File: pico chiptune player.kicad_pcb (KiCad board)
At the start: 4 copper layers, 80 x 70.8 mm, 31 parts, among them J1 MicroSD, J2 Speaker Out, SW1 Play / Pause, SW2 Next, SW3 Previous, U1 AY-3-8910, U2 PAM8302AAS, U3 0.96"OLED_I2C

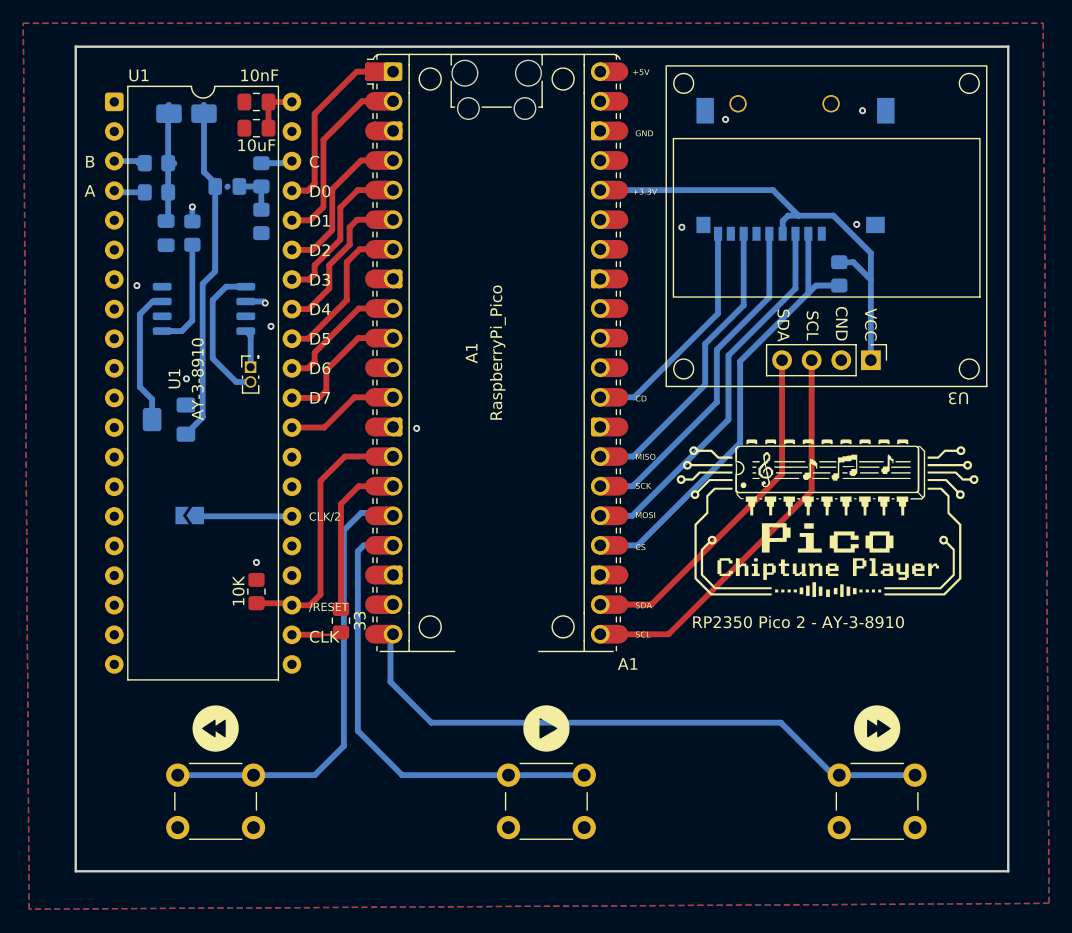
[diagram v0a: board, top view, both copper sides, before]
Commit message: docs, sch: rev 0.2 — align HARDWARE.md with schematic (SSOT)
Schematic is the single source of truth; HARDWARE.md updated to match:
- +5V rail sourced from Pico Pin 40 (VBUS), not Pin 39 (VSYS)
- Document R8 pull-up on PAM8302 ~SD; correct R3 as SD_CS pull-up
- PAM8302 pinout re-mapped to KiCad Amplifier_Audio:PAM8302AAS symbol
- Capacitor types (C3 polarized electrolytic, C4 MLCC ceramic)
  reflect actual schematic footprints
- Added Revision History section

Schematic-side changes (by Terence): no_connect markers on unused Pico
and AY-3-8910 pins, C1 footprint set. Title-block rev bumped 0.1 -> 0.2
in .kicad_sch and .kicad_pcb; date to 2026-08-12.

Co-Authored-By: Claude Opus 4.7 <noreply@anthropic.com>
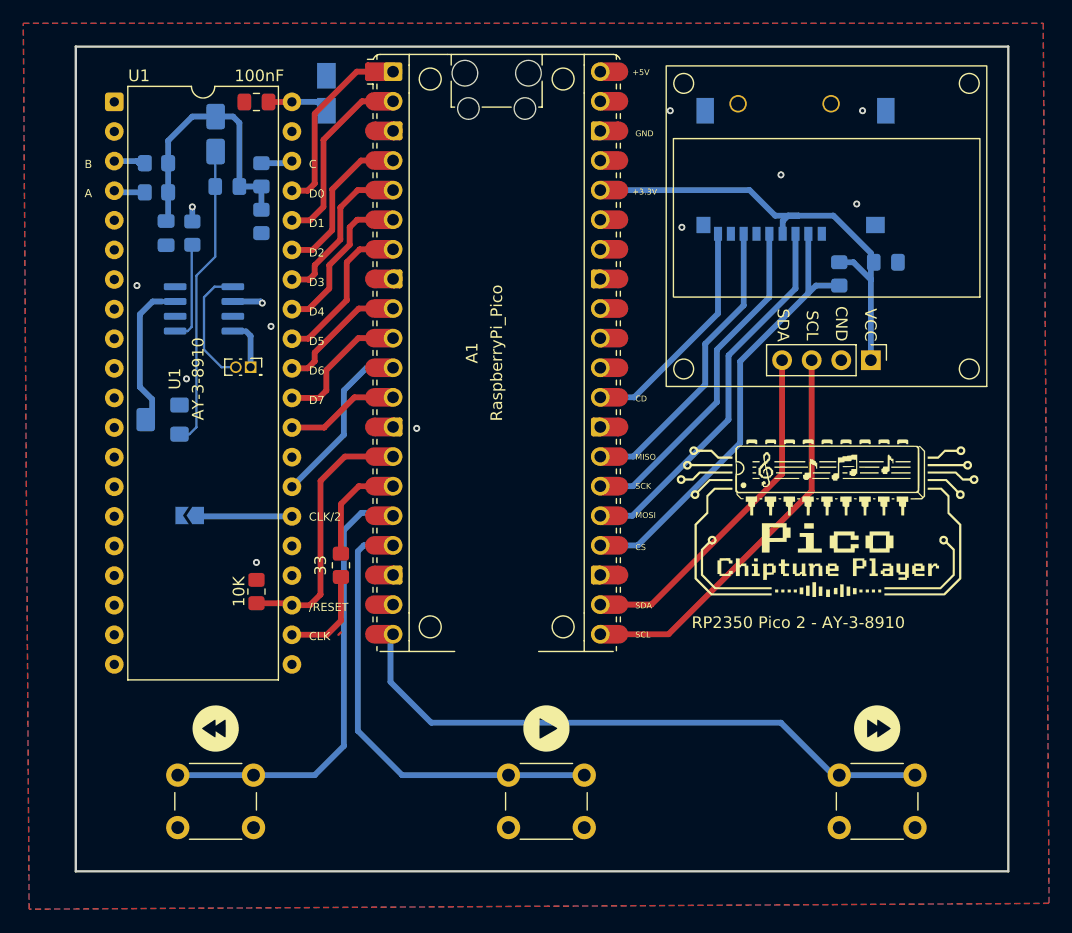
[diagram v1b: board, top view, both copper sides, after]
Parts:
- added C1: 10nF, Capacitor_SMD:C_0805_2012Metric_Pad1.18x1.45mm_HandSolder, B.Cu at (178.0, 91.0)
- C4: footprint Capacitor_SMD:C_0805_2012Metric_Pad1.18x1.45mm_HandSolder -> Capacitor_SMD:CP_Elec_3x5.3; moved to B.Cu
- C5: value 10nF -> 100nF
- J2: value Speaker Out -> Spk Out
- JP1: value Clk Div -> CLLK DIV
- U2: footprint Package_SO:SOIC-8_5.3x5.3mm_P1.27mm -> Package_SO:SOIC-8_3.9x4.9mm_P1.27mm
- moved C4 6.71 mm to (130.0, 76.5), turned to 90 degrees
- moved R2 4.75 mm to (131.2, 117.0)
- moved C3 3.05 mm to (120.5, 80.0), turned to -90 degrees
- moved RV1 0.55 mm to (116.0, 104.5)
- turned J2 to 0 degrees
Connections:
- U1 pad 27: +5V -> /BDIR
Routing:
- net /BDIR: track 0.00 -> 15.1 mm
- net Net-(C2-Pad1): track 14.5 -> 23.6 mm
- net Net-(A1-GPIO11): track 14.1 -> 9.36 mm
- net /CLOCK: track 4.99 -> 9.42 mm
- net Net-(C3-Pad2): track 29.7 -> 26.0 mm
- net +5V: track 7.86 -> 9.74 mm, vias 5 -> 2
- net Net-(J2-Pin_2): track 12.4 -> 10.7 mm
- net Net-(U2-~{SD}): track 9.46 -> 8.64 mm
- net GND: vias 6 -> 10
